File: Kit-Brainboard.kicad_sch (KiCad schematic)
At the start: 251 parts, among them J1 Pins_02x04_RightAngle_P2.54mm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, J2 Pins_02x05_P1.27mm_SMT, J3 USB_B_Micro_10118194-0011LF, Q1 MMBT3904, U1 PCM3060PW, U10 NJM2068, U11 NJM2068, U12 NJM2068, U13 NCP51460SN33, U14 DDR3L-RAM-4Gb_MT41K256M16TW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

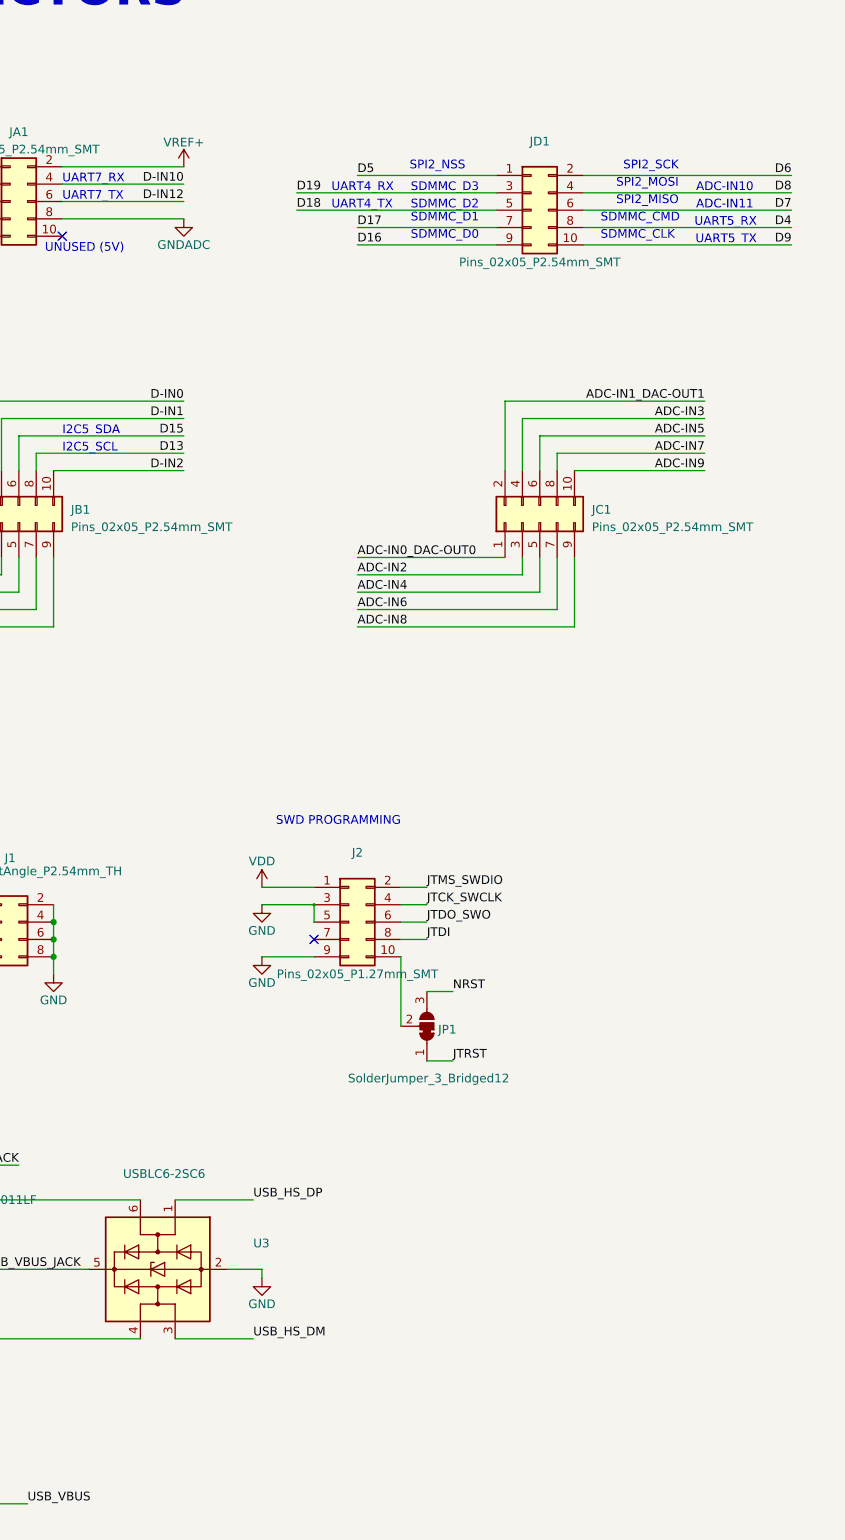
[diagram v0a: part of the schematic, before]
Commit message: Added USB pins: Changed JD4 to 2x6 header
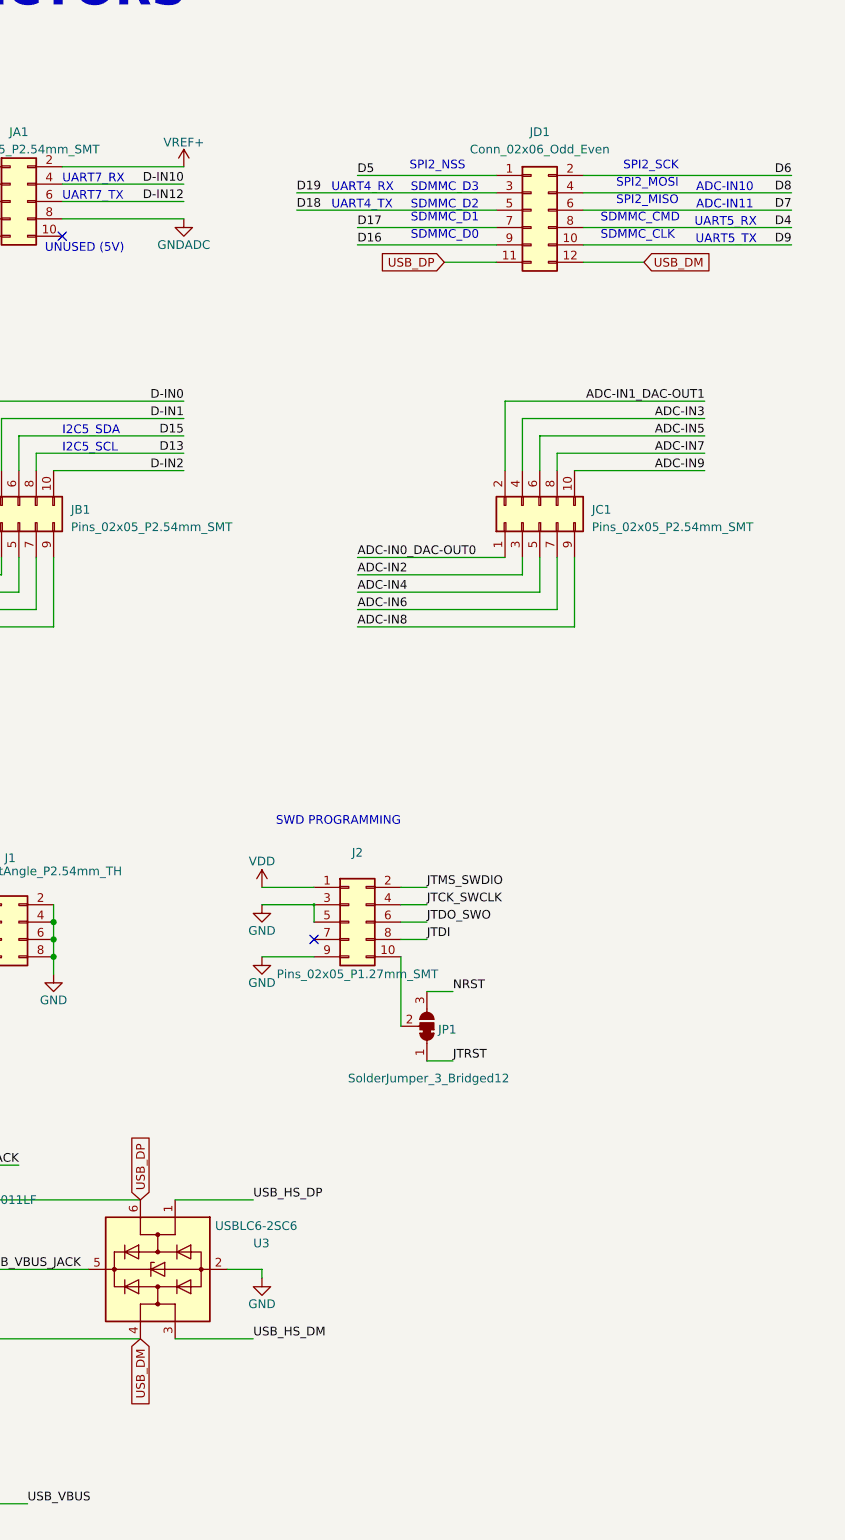
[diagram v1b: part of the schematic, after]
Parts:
- removed JD1: Pins_02x05_P2.54mm_SMT, Connector_PinHeader_2.54mm:PinHeader_2x05_P2.54mm_Vertical_SMD, symbol 4ms_Connector:Pins_02x05_P2.54mm_SMT
- added JD1: Conn_02x06_Odd_Even, Connector_PinHeader_2.54mm:PinHeader_2x06_P2.54mm_Vertical_SMD, symbol Connector_Generic:Conn_02x06_Odd_Even
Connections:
- net D16: now also JD1.9 (Pin_9)
- net D17: now also JD1.7 (Pin_7)
- net D18: now also JD1.5 (Pin_5)
- net D19: now also JD1.3 (Pin_3)
- net D4: now also JD1.8 (Pin_8)
- net D5: now also JD1.1 (Pin_1)
- net D6: now also JD1.2 (Pin_2)
- net D7: now also JD1.6 (Pin_6)
- net D8: now also JD1.4 (Pin_4)
- net D9: now also JD1.10 (Pin_10)
- net USB_DM: now reaches J3.2 (D-), U3.4 (I/O2)
- net USB_DM: now also JD1.12 (Pin_12)
- net USB_DP: now reaches J3.3 (D+), U3.6 (I/O1)
- net USB_DP: now also JD1.11 (Pin_11)
